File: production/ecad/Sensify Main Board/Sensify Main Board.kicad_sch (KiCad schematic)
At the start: 0 parts

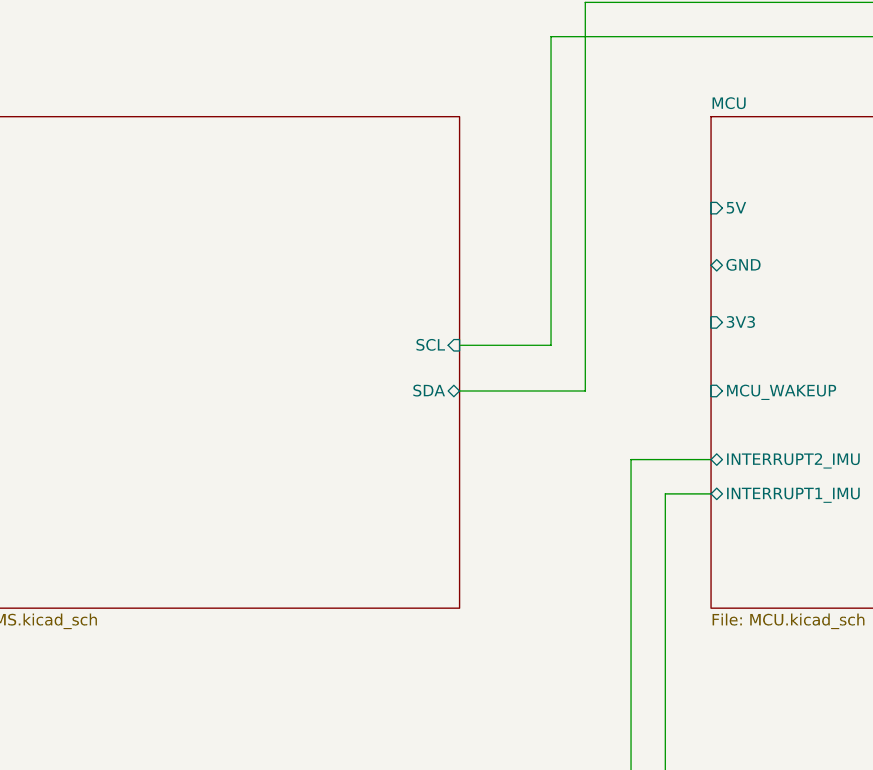
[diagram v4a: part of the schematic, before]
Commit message: Added switch footprints for MCU
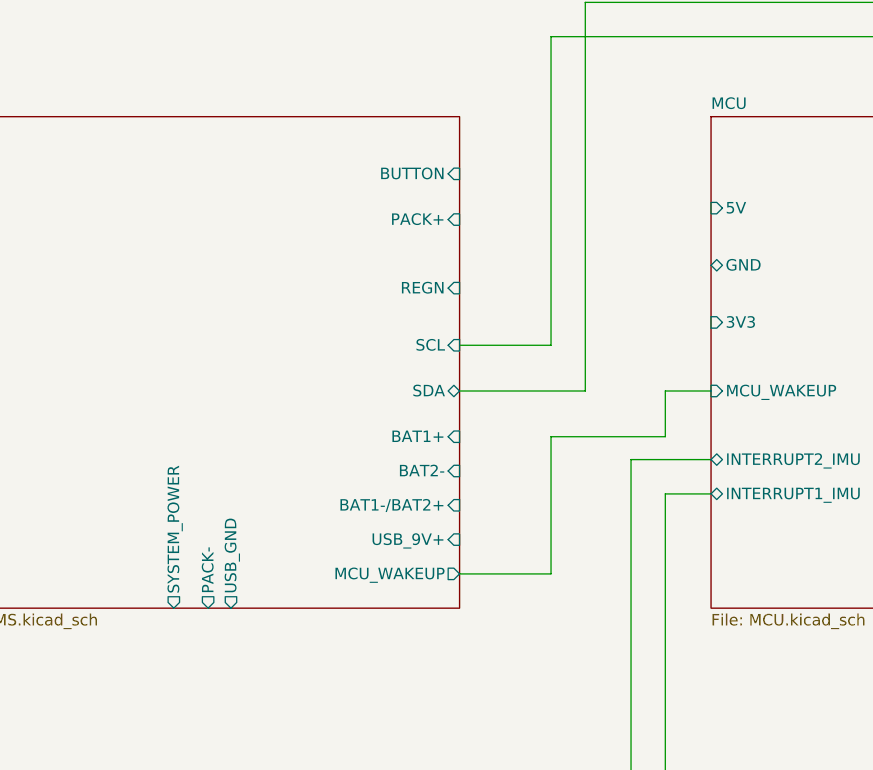
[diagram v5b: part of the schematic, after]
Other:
- sheet BMS ports: added BAT1+, BAT1-/BAT2+, BAT2-, BUTTON, MCU_WAKEUP, PACK+, PACK-, REGN, SYSTEM_POWER, USB_9V+, USB_GND; removed none
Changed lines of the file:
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@@
+    (stroke (width 0) (type default))
+  )
+  (wire (pts (xy 93.98 63.5) (xy 106.68 63.5))
     (stroke (width 0) (type default))
   )
@@
     (stroke (width 0) (type default))
   )
+  (wire (pts (xy 106.68 58.42) (xy 106.68 63.5))
+    (stroke (width 0) (type default))
+  )
   (wire (pts (xy 85.09 123.19) (xy 102.87 123.19))
     (stroke (width 0) (type default))
   )
   (wire (pts (xy 83.82 58.42) (xy 97.79 58.42))
+    (stroke (width 0) (type default))
+  )
+  (wire (pts (xy 93.98 63.5) (xy 93.98 78.74))
     (stroke (width 0) (type default))
   )
@@
     (stroke (width 0) (type default))
   )
+  (wire (pts (xy 83.82 78.74) (xy 93.98 78.74))
+    (stroke (width 0) (type default))
+  )
   (wire (pts (xy 102.87 66.04) (xy 111.76 66.04))
     (stroke (width 0) (type default))
@@
   )
   (wire (pts (xy 102.87 66.04) (xy 102.87 123.19))
+    (stroke (width 0) (type default))
+  )
+  (wire (pts (xy 106.68 58.42) (xy 111.76 58.42))
     (stroke (width 0) (type default))
   )
@@
       (effects (font (size 1.27 1.27)) (justify right))
     )
+    (pin "REGN" input (at 83.82 46.99 0)
+      (effects (font (size 1.27 1.27)) (justify right))
+    )
+    (pin "BAT1+" input (at 83.82 63.5 0)
+      (effects (font (size 1.27 1.27)) (justify right))
+    )
+    (pin "BAT2-" input (at 83.82 67.31 0)
+      (effects (font (size 1.27 1.27)) (justify right))
+    )
+    (pin "BAT1-{slash}BAT2+" input (at 83.82 71.12 0)
+      (effects (font (size 1.27 1.27)) (justify right))
+    )
+    (pin "USB_9V+" input (at 83.82 74.93 0)
+      (effects (font (size 1.27 1.27)) (justify right))
+    )
+    (pin "PACK+" input (at 83.82 39.37 0)
+      (effects (font (size 1.27 1.27)) (justify right))
+    )
+    (pin "BUTTON" input (at 83.82 34.29 0)
+      (effects (font (size 1.27 1.27)) (justify right))
+    )
+    (pin "MCU_WAKEUP" output (at 83.82 78.74 0)
+      (effects (font (size 1.27 1.27)) (justify right))
+    )
+    (pin "SYSTEM_POWER" output (at 52.07 82.55 270)
+      (effects (font (size 1.27 1.27)) (justify left))
+    )
+    (pin "PACK-" output (at 55.88 82.55 270)
+      (effects (font (size 1.27 1.27)) (justify left))
+    )
+    (pin "USB_GND" output (at 58.42 82.55 270)
+      (effects (font (size 1.27 1.27)) (justify left))
+    )
     (instances

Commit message: Improved MCU Schematic
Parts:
- added TP1, TP2, TP3, TP4, TP5: TestPoint, symbol Connector:TestPoint
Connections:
- new net +3V3: TP3.1
- new net +5V: TP4.1
- new net GND: TP5.1
- new net SCL: TP2.1
- new net SDA: TP1.1

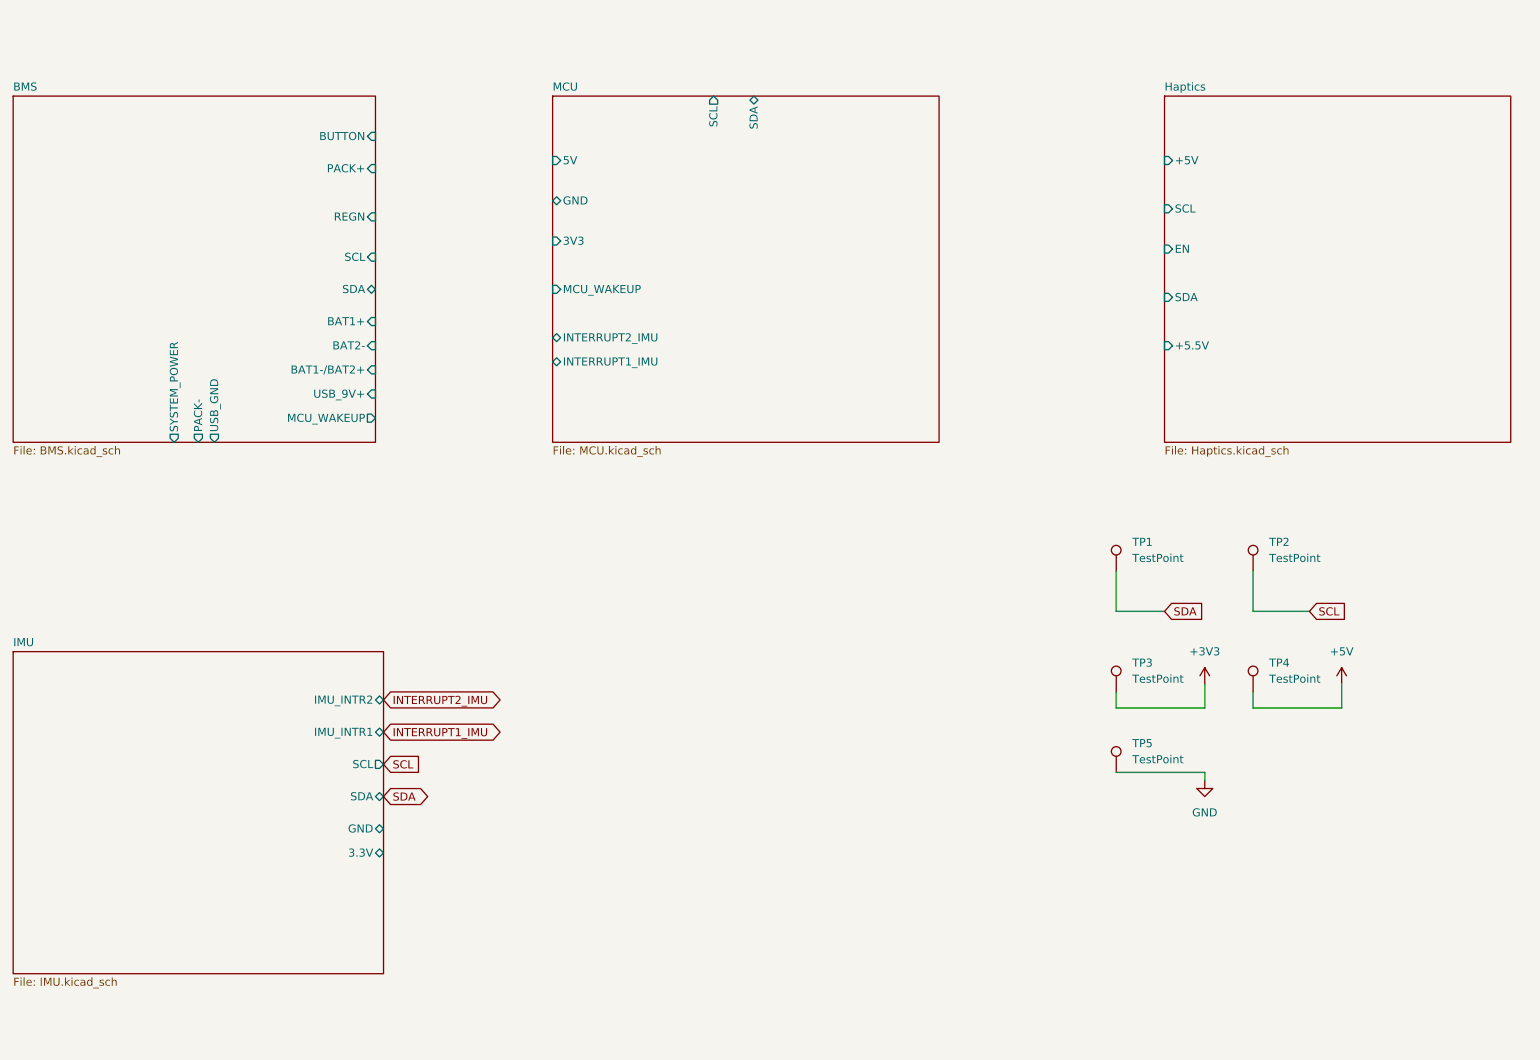
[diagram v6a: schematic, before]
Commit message: Finished Root Directory for IMU and Haptics
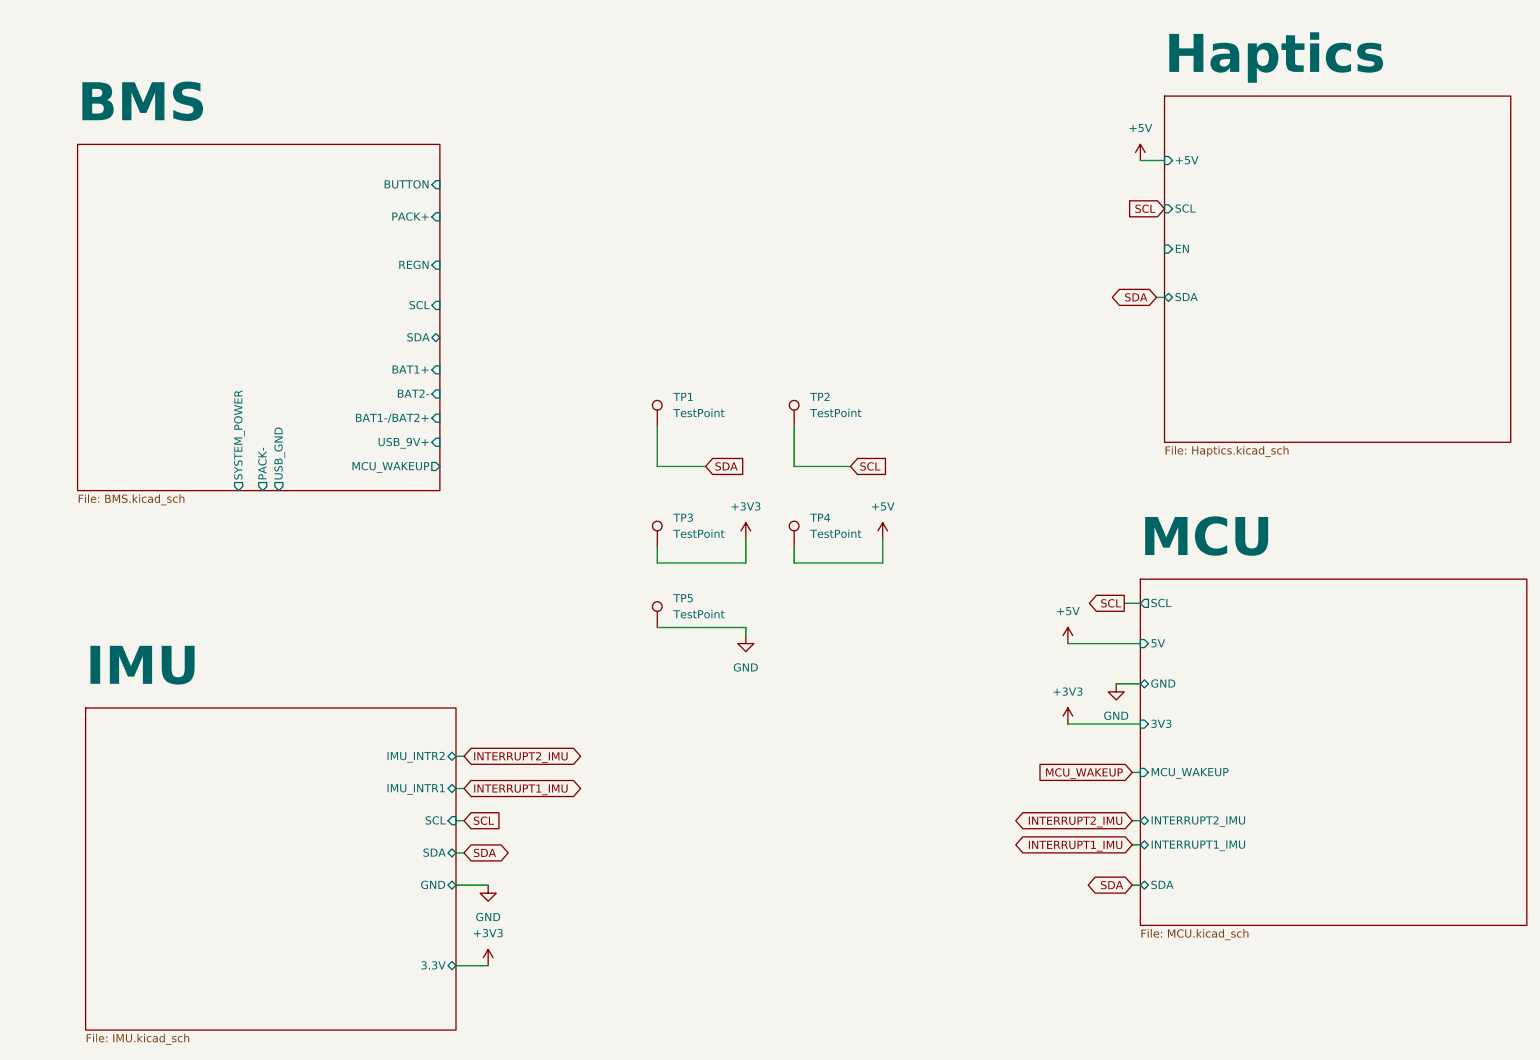
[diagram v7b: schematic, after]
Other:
- sheet Haptics ports: added none; removed +5.5V
- moved on the sheet: TP1, TP2, TP3, TP4, TP5

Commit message: Added Mounting Holes
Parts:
- added H1, H2, H3, H4: MountingHole, symbol Mechanical:MountingHole
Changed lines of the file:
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@@
+    )
+  )
+  (symbol (lib_id "Mechanical:MountingHole") (at 154.94 36.83 0) (unit 1)
+    (in_bom yes) (on_board yes) (dnp no) (fields_autoplaced)
+    (property "Reference" "H2" (at 157.48 35.56 0)
+      (effects (font (size 1.27 1.27)) (justify left))
+    )
+    (property "Value" "MountingHole" (at 157.48 38.1 0)
+      (effects (font (size 1.27 1.27)) (justify left))
+    )
+    (property "Footprint" "" (at 154.94 36.83 0)
+      (effects (font (size 1.27 1.27)) hide)
+    )
+    (property "Datasheet" "~" (at 154.94 36.83 0)
+      (effects (font (size 1.27 1.27)) hide)
+    )
+    (instances
+      (project "Sensify Main Board"
+        (path "/9a7ba7c3-7d28-4a83-bdbc-38fbff59fcbe"
+          (reference "H2") (unit 1)
+        )
+      )
     )
   )
@@
     )
   )
+  (symbol (lib_id "Mechanical:MountingHole") (at 129.54 36.83 0) (unit 1)
+    (in_bom yes) (on_board yes) (dnp no) (fields_autoplaced)
+    (property "Reference" "H1" (at 132.08 35.56 0)
+      (effects (font (size 1.27 1.27)) (justify left))
+    )
+    (property "Value" "MountingHole" (at 132.08 38.1 0)
+      (effects (font (size 1.27 1.27)) (justify left))
+    )
+    (property "Footprint" "" (at 129.54 36.83 0)
+      (effects (font (size 1.27 1.27)) hide)
+    )
+    (property "Datasheet" "~" (at 129.54 36.83 0)
+      (effects (font (size 1.27 1.27)) hide)
+    )
+    (instances
+      (project "Sensify Main Board"
+        (path "/9a7ba7c3-7d28-4a83-bdbc-38fbff59fcbe"
+          (reference "H1") (unit 1)
+        )
+      )
+    )
+  )
+  (symbol (lib_id "Mechanical:MountingHole") (at 154.94 48.26 0) (unit 1)
+    (in_bom yes) (on_board yes) (dnp no) (fields_autoplaced)
+    (property "Reference" "H4" (at 157.48 46.99 0)
+      (effects (font (size 1.27 1.27)) (justify left))
+    )
+    (property "Value" "MountingHole" (at 157.48 49.53 0)
+      (effects (font (size 1.27 1.27)) (justify left))
+    )
+    (property "Footprint" "" (at 154.94 48.26 0)
+      (effects (font (size 1.27 1.27)) hide)
+    )
+    (property "Datasheet" "~" (at 154.94 48.26 0)
+      (effects (font (size 1.27 1.27)) hide)
+    )
+    (instances
+      (project "Sensify Main Board"
+        (path "/9a7ba7c3-7d28-4a83-bdbc-38fbff59fcbe"
+          (reference "H4") (unit 1)
+        )
+      )
+    )
+  )
   (symbol (lib_id "power:+3V3") (at 142.24 97.79 0) (unit 1)
     (in_bom yes) (on_board yes) (dnp no) (fields_autoplaced)
@@
         )
       )
+    )
+  )
+  (symbol (lib_id "Mechanical:MountingHole") (at 129.54 48.26 0) (unit 1)
+    (in_bom yes) (on_board yes) (dnp no) (fields_autoplaced)
+    (property "Reference" "H3" (at 132.08 46.99 0)
+      (effects (font (size 1.27 1.27)) (justify left))
+    )
+    (property "Value" "MountingHole" (at 132.08 49.53 0)
+      (effects (font (size 1.27 1.27)) (justify left))
+    )
+    (property "Footprint" "" (at 129.54 48.26 0)
+      (effects (font (size 1.27 1.27)) hide)
+    )
+    (property "Datasheet" "~" (at 129.54 48.26 0)
+      (effects (font (size 1.27 1.27)) hide)
+    )
+    (instances
+      (project "Sensify Main Board"
+        (path "/9a7ba7c3-7d28-4a83-bdbc-38fbff59fcbe"
+          (reference "H3") (unit 1)
+        )
+      )
